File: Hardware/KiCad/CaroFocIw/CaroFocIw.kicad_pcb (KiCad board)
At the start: 4 copper layers, 92 x 42 mm, 111 parts, among them J1 Conn_01x04, J10 Conn_01x03, J11 Conn_01x03, J12 Conn_01x03, J13 Conn_01x03, J14 Conn_01x03, J15 Conn_01x04, J16 Conn_01x04, J17 Conn_01x04, J18 Conn_01x04, J19 Conn_01x04, J2 Conn_01x01, J20 Conn_01x04, J21 Conn_01x02, J22 Conn_01x02, J3 Conn_01x01, J4 Conn_01x01, J5 Conn_01x02, J6 Conn_01x01, J7 Conn_01x02, J8 Conn_01x02, J9 Conn_01x03, Q1 Q_NMOS_SGD, Q2 Q_NMOS_SGD, Q3 Q_NMOS_SGD, Q4 Q_NMOS_SGD, Q5 Q_NMOS_SGD, Q6 Q_NMOS_SGD, U1 TCAN332, U2 STM32F405RGTx, U3 TLE7185-1E, U4 ACS711xEXLT-15AB, U5 AS5048A, U6 ACS711xEXLT-15AB, U7 ACS711xEXLT-15AB, U8 LMR16006YQ3

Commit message: more routing
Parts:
- removed H3, H4: MountingHole_Pad, MountingHole:MountingHole_3.2mm_M3_ISO14580_Pad
- removed J5: Conn_01x02, Pin_Headers:Pin_Header_Straight_1x02_Pitch2.00mm
- removed J6: Conn_01x01, TestPoint:TestPoint_Pad_D3.0mm
- added J23: Conn_01x04, Connector_JST:JST_GH_BM04B-GHS-TBT_1x04-1MP_P1.25mm_Vertical, F.Cu at (217.5, 35.0)
- moved R13 33.4 mm to (168.6, 20.6), turned to 45 degrees
- moved R11 30.8 mm to (147.2, 27.2), turned to 45 degrees
- moved R9 29.9 mm to (166.0, 23.4), turned to 45 degrees
- moved R8 29.5 mm to (148.4, 29.0), turned to 135 degrees
- moved C17 29.0 mm to (170.0, 69.0)
- moved C23 27.0 mm to (150.0, 40.9)
- moved C24 27.0 mm to (147.0, 47.5)
- moved C25 27.0 mm to (152.0, 46.5)
- moved D1 27.0 mm to (150.0, 48.0)
- moved L1 27.0 mm to (151.5, 43.5)
- moved U8 27.0 mm to (147.5, 43.5)
- moved U1 26.4 mm to (163.0, 19.6), turned to 45 degrees
- moved R1 26.1 mm to (164.8, 17.8)
- moved C1 26.1 mm to (161.2, 21.4), turned to 135 degrees
- moved C9 15.9 mm to (172.8, 43.0), turned to 90 degrees
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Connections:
- H1 pad 1: GNDPWR_A -> GND
- H2 pad 1: GNDPWR_A -> GND
- H5 pad 1: Net-(H5-Pad1) -> GND
- H6 pad 1: Net-(H6-Pad1) -> GND
- U1 pad 5: Net-(U1-Pad5) -> (no net)
- U1 pad 8: Net-(U1-Pad8) -> (no net)
- U2 pad 11: Net-(U2-Pad11) -> (no net)
- U2 pad 14: Net-(U2-Pad14) -> (no net)
- U2 pad 15: Net-(U2-Pad15) -> (no net)
- U2 pad 16: Net-(U2-Pad16) -> (no net)
- U2 pad 17: Net-(U2-Pad17) -> (no net)
- U2 pad 2: Net-(U2-Pad2) -> (no net)
- U2 pad 24: Net-(U2-Pad24) -> (no net)
- U2 pad 25: Net-(U2-Pad25) -> (no net)
- U2 pad 26: Net-(U2-Pad26) -> (no net)
- U2 pad 27: Net-(U2-Pad27) -> (no net)
- U2 pad 28: Net-(U2-Pad28) -> (no net)
- U2 pad 29: Net-(U2-Pad29) -> (no net)
- U2 pad 3: Net-(U2-Pad3) -> (no net)
- U2 pad 31: Net-(U2-Pad31) -> (no net)
- U2 pad 33: Net-(U2-Pad33) -> (no net)
- U2 pad 34: /GateDriver/LogicWL -> /GateDriver/LogicUL
- U2 pad 36: /GateDriver/LogicUL -> /GateDriver/LogicWL
- U2 pad 37: Net-(U2-Pad37) -> (no net)
- U2 pad 38: Net-(U2-Pad38) -> (no net)
- U2 pad 39: Net-(U2-Pad39) -> (no net)
- U2 pad 4: Net-(U2-Pad4) -> (no net)
- U2 pad 40: Net-(U2-Pad40) -> (no net)
- U2 pad 41: /MCU/LogicWH -> /MCU/LogicUH
- U2 pad 43: /MCU/LogicUH -> /MCU/LogicWH
- U2 pad 44: Net-(U2-Pad44) -> (no net)
- U2 pad 45: Net-(U2-Pad45) -> (no net)
- U2 pad 47: Net-(U2-Pad47) -> (no net)
- U2 pad 5: Net-(U2-Pad5) -> (no net)
- U2 pad 50: Net-(U2-Pad50) -> (no net)
- U2 pad 51: Net-(U2-Pad51) -> (no net)
- U2 pad 52: Net-(U2-Pad52) -> (no net)
- U2 pad 53: Net-(U2-Pad53) -> (no net)
- U2 pad 54: Net-(U2-Pad54) -> (no net)
- U2 pad 58: Net-(U2-Pad58) -> (no net)
- U2 pad 59: Net-(U2-Pad59) -> (no net)
- U2 pad 6: Net-(U2-Pad6) -> (no net)
- U3 pad 1: GND_B -> (no net)
- U5 pad 10: Net-(U5-Pad10) -> (no net)
- U5 pad 14: Net-(U5-Pad14) -> (no net)
- U5 pad 5: Net-(U5-Pad5) -> (no net)
- U5 pad 6: Net-(U5-Pad6) -> (no net)
- U5 pad 7: Net-(U5-Pad7) -> (no net)
- U5 pad 8: Net-(U5-Pad8) -> (no net)
- U5 pad 9: Net-(U5-Pad9) -> (no net)
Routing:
- net /MCU/CurrentW: track 5.16 -> 43.0 mm, vias 0 -> 1
- net /Can/CanTx: track 33.5 -> 3.76 mm, vias 2 -> 0
- net /MCU/CurrentU: track 4.95 -> 33.0 mm, vias 0 -> 1
- net /Can/CanRx: track 29.5 -> 5.10 mm, vias 2 -> 0
- net /MCU/LogicUH: track 11.2 -> 26.9 mm, vias 0 -> 2
- net /MCU/LogicVH: track 10.9 -> 25.9 mm
- net /MCU/LogicWH: track 10.0 -> 25.1 mm
- net /GateDriver/LogicUL: track 11.7 -> 24.6 mm, vias 0 -> 2
- net /GateDriver/LogicVL: track 11.0 -> 23.7 mm, vias 0 -> 2
- net /GateDriver/LogicWL: track 10.3 -> 22.9 mm, vias 0 -> 2
- net /GateDriver/SourceUL: track 0.00 -> 10.7 mm, vias 0 -> 1
- net /MCU/GateDriverEnable: track 19.6 -> 9.23 mm, vias 0 -> 1
- net Net-(R7-Pad1): track 10.1 -> 1.85 mm, vias 0 -> 1
- net Net-(R6-Pad1): track 9.79 -> 1.89 mm, vias 0 -> 1
- net Net-(R2-Pad2): track 7.44 -> 0.00 mm
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- added copper zone on F.Cu, net GNDA
- removed copper zone on B.Cu, net GNDPWR_A
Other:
- outline, holes or cut-outs redrawn

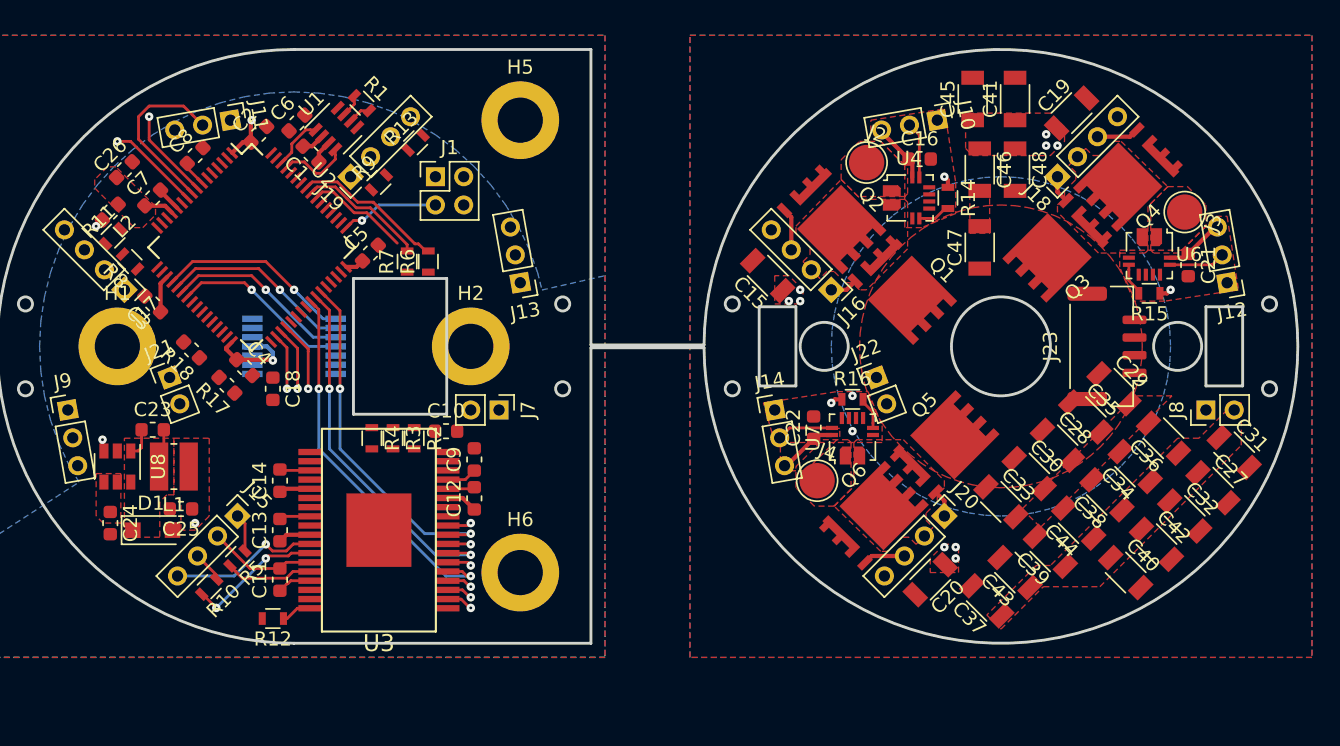
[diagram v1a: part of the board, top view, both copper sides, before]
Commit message: Routing (seems to be) done, should be reviewed before production
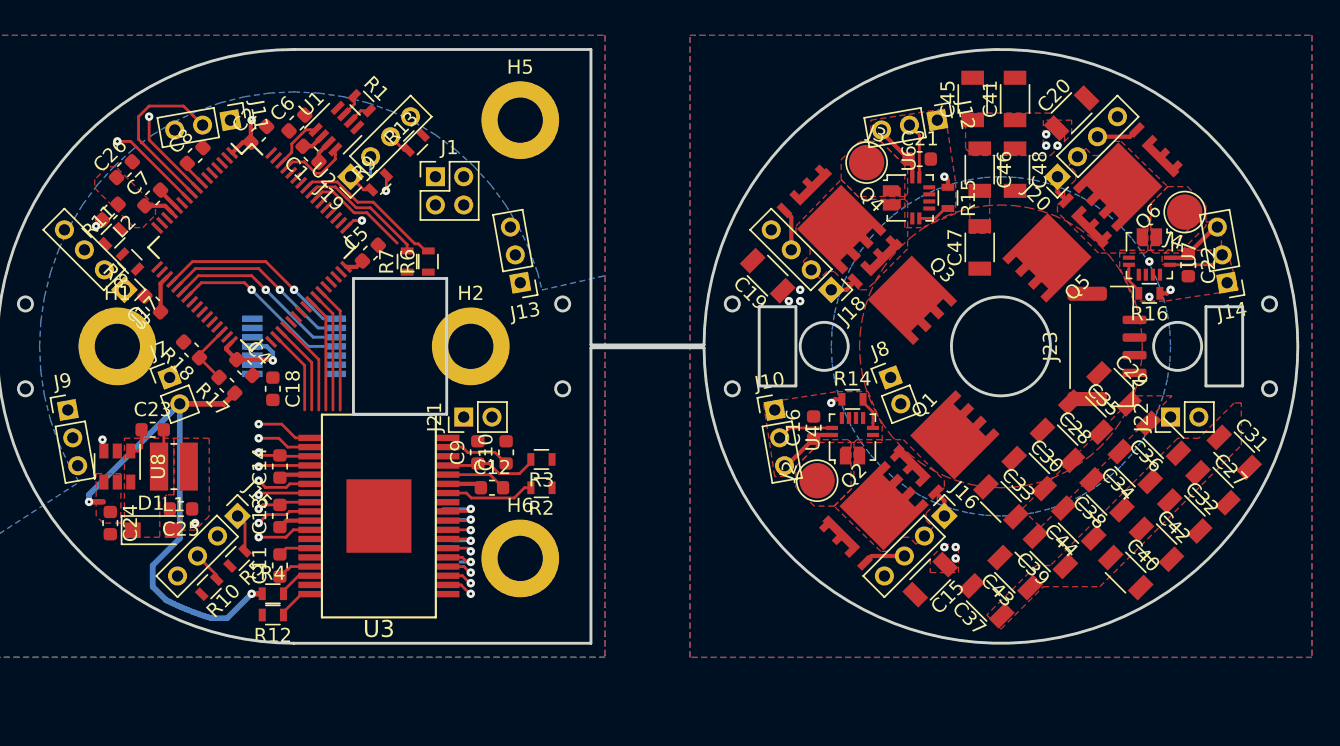
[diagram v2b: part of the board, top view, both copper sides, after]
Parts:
- moved C20 34.5 mm to (215.0, 18.5), turned to 45 degrees
- moved J14 33.2 mm to (226.0, 30.5), turned to 190 degrees
- moved J4 32.2 mm to (223.0, 25.5), turned to 160 degrees
- moved Q6 30.0 mm to (219.0, 23.0), turned to 135 degrees
- moved C22 28.9 mm to (223.2, 29.2), turned to 270 degrees
- moved J20 25.3 mm to (214.0, 23.0), turned to 135 degrees
- moved U7 24.7 mm to (220.5, 28.5), turned to 270 degrees
- moved C15 24.4 mm to (205.0, 51.5), turned to 225 degrees
- moved C19 24.4 mm to (193.5, 30.0), turned to 135 degrees
- moved J10 23.5 mm to (194.0, 39.5), turned to 10 degrees
- moved J12 23.5 mm to (205.5, 19.0), turned to 280 degrees
- moved J7 23.4 mm to (151.2, 37.2), turned to 21 degrees
- moved J2 22.8 mm to (197.0, 44.5), turned to 70 degrees
- moved J3 22.8 mm to (200.5, 22.0), turned to 340 degrees
- moved J8 22.4 mm to (202.2, 37.2), turned to 21 degrees
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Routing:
- net BattA: track 0.00 -> 37.6 mm, vias 0 -> 2
- net /GateDriver/GateWHbR: track 0.00 -> 18.7 mm, vias 0 -> 2
- net /GateDriver/LogicUL: track 24.6 -> 7.74 mm, vias 2 -> 1
- net /MCU/LogicUH: track 26.9 -> 10.6 mm, vias 2 -> 1
- net /MCU/LogicVH: track 25.9 -> 11.4 mm, vias 2 -> 1
- net /GateDriver/LogicVL: track 23.7 -> 9.57 mm, vias 2 -> 1
- net /MCU/LogicWH: track 25.1 -> 12.3 mm, vias 2 -> 1
- net /GateDriver/LogicWL: track 22.9 -> 10.5 mm, vias 2 -> 1
- net /GateDriver/Gate_U_L_bR: track 9.67 -> 0.00 mm, vias 2 -> 0
- net /GateDriver/SourceUL: track 10.7 -> 3.85 mm
- net Net-(R2-Pad2): track 0.00 -> 6.33 mm
- net /GateDriver/GateUHbR: track 6.22 -> 0.00 mm
- net /MCU/SWCLK: track 6.75 -> 1.33 mm
- net /GateDriver/SourceUH: track 7.68 -> 2.32 mm
- net Net-(C9-Pad1): track 2.15 -> 6.77 mm
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
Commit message: forgot to save
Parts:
- removed C29, C35, C36: C, Capacitors_SMD:C_1206
- moved C17 32.6 mm to (160.0, 38.0), turned to 270 degrees
- moved R6 14.5 mm to (178.0, 40.8)
- moved R7 14.5 mm to (176.5, 40.8)
- moved J1 4.00 mm to (170.0, 27.0), turned to 270 degrees
- moved J8 0.95 mm to (201.2, 37.2)
- moved R8 0.43 mm to (148.8, 28.8), turned to 45 degrees
- moved R13 0.18 mm to (168.5, 20.8)
- moved R9 0.15 mm to (166.0, 23.2)
- moved R11 0.07 mm to (147.2, 27.2)
- moved J7 0.07 mm to (151.2, 37.2)
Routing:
- net /MCU/GateDriverEnable: track 9.23 -> 50.5 mm, vias 1 -> 2
- net /Can/CanH: track 1.62 -> 36.8 mm, vias 0 -> 3
- net /Can/CanL: track 1.62 -> 35.9 mm
- net /GateDriver/SourceWL: track 4.04 -> 35.5 mm
- net BattA: track 37.6 -> 68.5 mm, vias 2 -> 4
- net /GateDriver/Gate_W_L_bR: track 3.89 -> 34.7 mm, vias 1 -> 2
- net /GateDriver/SourceWH: track 5.06 -> 32.8 mm
- net /GateDriver/SourceVL: track 3.94 -> 31.0 mm
- net /GateDriver/Gate_V_L_bR: track 3.69 -> 27.5 mm, vias 1 -> 2
- net /GateDriver/SourceVH: track 3.83 -> 27.6 mm
- net /GateDriver/GateVHbR: track 3.98 -> 27.5 mm, vias 1 -> 2
- net /MCU/~RST: track 1.82 -> 22.2 mm, vias 0 -> 1
- net Net-(R7-Pad1): track 1.85 -> 22.1 mm, vias 1 -> 0
- net Net-(R6-Pad1): track 1.89 -> 21.9 mm, vias 1 -> 0
- net /MCU/~GateDriverErr1: track 9.11 -> 27.5 mm
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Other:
- outline, holes or cut-outs redrawn

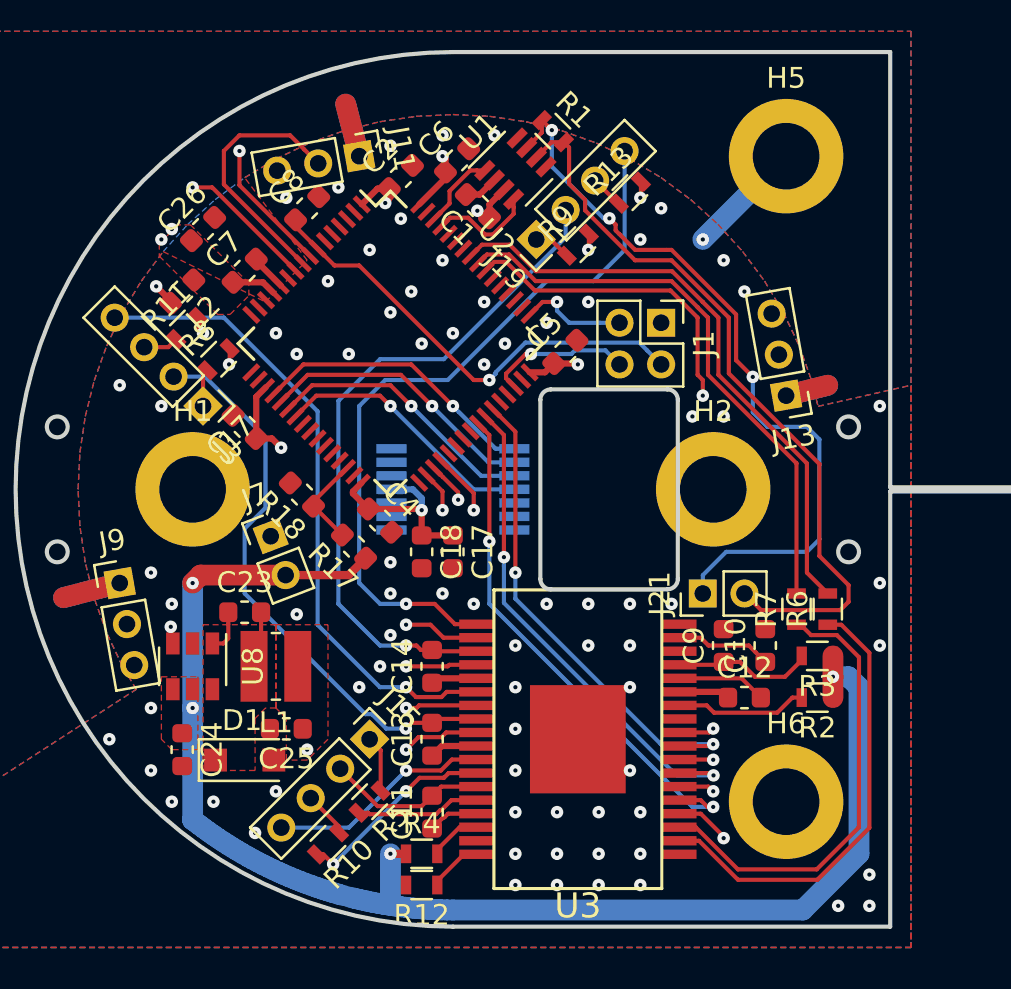
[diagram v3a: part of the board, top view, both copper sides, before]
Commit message: routing done, some via stitching and panelizing to do
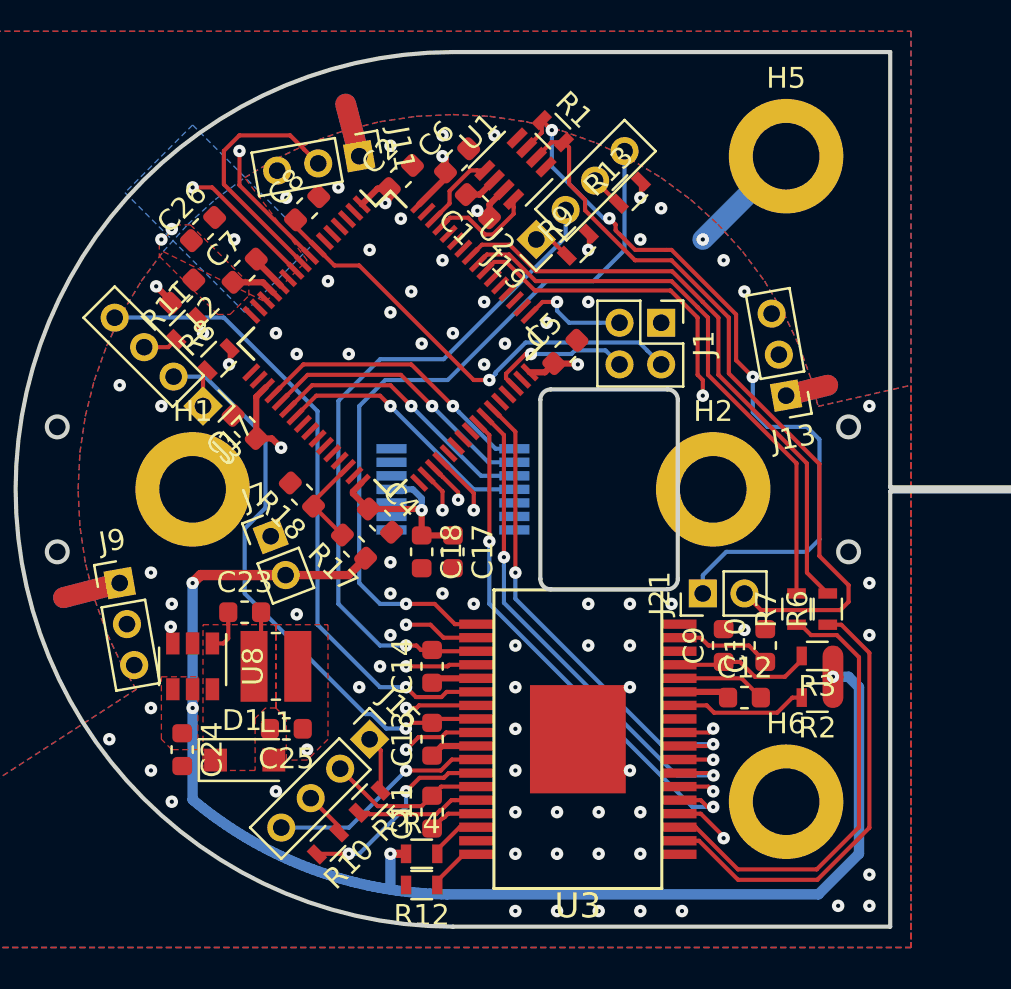
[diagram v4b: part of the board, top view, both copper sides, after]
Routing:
- net BattA: track 68.5 -> 66.8 mm
- net /MCU/CurrentU: track 33.0 -> 31.9 mm
- net +3.3VA: track 5.06 -> 4.50 mm
- net GNDA: vias 0 -> 1
- net GND: vias 77 -> 74

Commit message: some panelizing
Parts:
- moved C15 6.00 mm to (199.0, 51.5)
- moved C16 6.00 mm to (190.8, 40.8)
- moved C19 6.00 mm to (187.5, 30.0)
- moved C20 6.00 mm to (209.0, 18.5)
- moved C21 6.00 mm to (198.2, 21.8)
- moved C22 6.00 mm to (217.2, 29.2)
- moved C27 6.00 mm to (219.0, 45.0)
- moved C28 6.00 mm to (208.0, 42.0)
- moved C30 6.00 mm to (206.0, 44.0)
- moved C31 6.00 mm to (220.5, 42.5)
- moved C32 6.00 mm to (217.0, 47.0)
- moved C33 6.00 mm to (204.0, 46.0)
- moved C34 6.00 mm to (213.5, 43.5)
- moved C37 6.00 mm to (203.0, 53.0)
- moved C38 6.00 mm to (211.5, 45.5)
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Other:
- board size 92 x 42 mm -> 86 x 42 mm

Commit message: preliminary version 1.0
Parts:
- removed the C31 at (220.5, 42.5)
- removed the C37 at (203.0, 53.0)
- removed the C41 at (205.0, 17.5)
- removed H5, H6: MountingHole_Pad, MountingHole:MountingHole_3.2mm_M3_ISO14580_Pad
- removed J21: Conn_01x02, Connector_PinHeader_2.00mm:PinHeader_1x02_P2.00mm_Vertical
- removed J23: Conn_01x04, Connector_JST:JST_GH_BM04B-GHS-TBT_1x04-1MP_P1.25mm_Vertical
- removed the J8 at (195.2, 37.2)
- removed the U1 at (163.0, 19.6)
- removed the U8 at (147.5, 43.5)
- added C29: 10µ 35V, Capacitor_SMD:C_1206_3216Metric, F.Cu at (46.0, 9.00)
- added C34: 10µ 35V, Capacitor_SMD:C_1206_3216Metric, F.Cu at (43.0, 18.0)
- added C38: 10µ 35V, Capacitor_SMD:C_1206_3216Metric, F.Cu at (45.0, -17.5)
- added G***: LOGO, libs:CDLC-Logo, B.Cu at (53.0, 16.0)
- added H3: MountingHole_Pad, MountingHole:MountingHole_3.2mm_M3_ISO14580_Pad, F.Cu at (16.0, -16.0)
- added H4: MountingHole_Pad, MountingHole:MountingHole_3.2mm_M3_ISO14580_Pad, F.Cu at (16.0, 16.0)
- added J2: Conn_01x01, TestPoint:TestPoint_Pad_D2.5mm, F.Cu at (34.5, -13.0)
- added J5: Conn_01x02, Connector_PinHeader_2.00mm:PinHeader_1x02_P2.00mm_Vertical, F.Cu at (-8.75, 2.25)
- added J6: Conn_01x02, Connector_PinHeader_2.00mm:PinHeader_1x02_P2.00mm_Vertical, F.Cu at (35.2, 2.25)
- added NT1: Net-Tie_2, NetTie:NetTie-2_SMD_Pad0.5mm, B.Cu at (-8.25, -10.2)
- added REF**: OSHW-Logo2_7.3x6mm_SilkScreen, Symbol:OSHW-Logo2_7.3x6mm_SilkScreen, B.Cu at (51.0, 4.00)
- added U5: ACS711xEXLT-15AB, Sensor_Current:Allegro_QFN-12-10-1EP_3x3mm_P0.5mm, F.Cu at (33.5, 6.50)
- added U9: LMR16006YQ3, Package_TO_SOT_SMD:SOT-23-6, F.Cu at (-12.5, 8.50)
- C10: value 2,2µ -> 4.7µ 25V
- C11, C12, C13, C14: value 1µ -> 4.7µ 25V
- C15, C19, C20: value 22μ, 25V -> 10μ 35V; footprint Capacitors_SMD:C_1206 -> Capacitor_SMD:C_1206_3216Metric
- C18, C25, C26: value 10μ -> 10μ 6.3V
- C2, C3, C4, C5, C6: value 2.2μ -> 4.7µ, 6.3V
- C24: value 10μ -> 10μ 35V
- C27, C28, C30: value C -> 10µ 35V; footprint Capacitors_SMD:C_1206 -> Capacitor_SMD:C_1206_3216Metric
- C31: renamed from C32; value C -> 10µ 35V; footprint Capacitors_SMD:C_1206 -> Capacitor_SMD:C_1206_3216Metric
- C32: renamed from C33; value C -> 10µ 35V; footprint Capacitors_SMD:C_1206 -> Capacitor_SMD:C_1206_3216Metric
- C33: renamed from C34; value C -> 10µ 35V; footprint Capacitors_SMD:C_1206 -> Capacitor_SMD:C_1206_3216Metric
- C35: renamed from C38; value C -> 10µ 35V; footprint Capacitors_SMD:C_1206 -> Capacitor_SMD:C_1206_3216Metric
- C36: renamed from C39; value C -> 10µ 35V; footprint Capacitors_SMD:C_1206 -> Capacitor_SMD:C_1206_3216Metric
- C37: renamed from C40; value C -> 10µ 35V; footprint Capacitors_SMD:C_1206 -> Capacitor_SMD:C_1206_3216Metric
- C39: renamed from C42; value C -> 10µ 35V; footprint Capacitors_SMD:C_1206 -> Capacitor_SMD:C_1206_3216Metric
- C40: renamed from C43; value C -> 10µ 35V; footprint Capacitors_SMD:C_1206 -> Capacitor_SMD:C_1206_3216Metric
- C41: renamed from C44; value C -> 10µ 35V; footprint Capacitors_SMD:C_1206 -> Capacitor_SMD:C_1206_3216Metric
- C42: renamed from C45; value C -> 10µ 35V; footprint Capacitors_SMD:C_1206 -> Capacitor_SMD:C_1206_3216Metric
- C43: renamed from C46; value C -> 10µ 35V; footprint Capacitors_SMD:C_1206 -> Capacitor_SMD:C_1206_3216Metric
- C44: renamed from C47; value C -> 10µ 35V; footprint Capacitors_SMD:C_1206 -> Capacitor_SMD:C_1206_3216Metric
- C45: renamed from C48; value C -> 10µ 35V; footprint Capacitors_SMD:C_1206 -> Capacitor_SMD:C_1206_3216Metric
- C7: value 10μ -> 4.7µ, 6.3V
- C9: value 2,2µ -> 4.7µ 35V
- D1: footprint Diodes_SMD:D_SOD-123F -> Diode_SMD:D_SOD-123F
- J13: value Conn_01x03 -> Conn_01x04; footprint Connector_PinHeader_2.00mm:PinHeader_1x03_P2.00mm_Vertical -> Connector_PinHeader_2.00mm:PinHeader_1x04_P2.00mm_Vertical
- J19: value Conn_01x04 -> Conn_01x02; footprint Connector_PinHeader_2.00mm:PinHeader_1x04_P2.00mm_Vertical -> Connector_PinHeader_2.00mm:PinHeader_1x02_P2.00mm_Vertical
- J4: value Conn_01x01 -> Conn_01x04_MountingPin; footprint TestPoint:TestPoint_Pad_D2.5mm -> Connector_JST:JST_GH_BM04B-GHS-TBT_1x04-1MP_P1.25mm_Vertical
- J7: value Conn_01x02 -> Conn_01x03; footprint Connector_PinHeader_2.00mm:PinHeader_1x02_P2.00mm_Vertical -> Connector_PinHeader_2.00mm:PinHeader_1x03_P2.00mm_Vertical
- L1: footprint Inductors_SMD:L_Wuerth_MAPI-3015 -> Inductor_SMD:L_Wuerth_MAPI-3015
- Q1, Q2, Q3, Q4, Q5, Q6: value Q_NMOS_SGD -> BSZ013NE2LS5I; footprint libs:TDSON-8_FL -> libs:PG-TSDSON-8-FL
- R1, R10, R11, R12, R13, R14, R15, R16, R2, R3, R4, R5, R8, R9: footprint Resistors_SMD:R_0603 -> Resistor_SMD:R_0603_1608Metric
- R6, R7: value 4.7k -> 10k; footprint Resistors_SMD:R_0603 -> Resistor_SMD:R_0603_1608Metric
- U2: value STM32F405RGTx -> TCAN332; footprint Package_QFP:LQFP-64_10x10mm_P0.5mm -> Package_TO_SOT_SMD:SOT-23-8
- U3: value TLE7185-1E -> STM32F405RGTx; footprint libs:PG-DSO-36-38 -> Package_QFP:LQFP-64_10x10mm_P0.5mm
- U4: value ACS711xEXLT-15AB -> TLE7185-1E; footprint Sensor_Current:Allegro_QFN-12-10-1EP_3x3mm_P0.5mm -> libs:PG-DSO-36-38
- moved U4 189.8 mm to (6.00, 12.0)
- moved J13 180.9 mm to (-4.00, 12.0), turned to 315 degrees
- moved U3 177.4 mm to (-3.00, -7.00), turned to 315 degrees
- moved J15 175.6 mm to (-12.0, -4.00), turned to 225 degrees
- moved J7 170.4 mm to (-16.0, 4.50), turned to 10 degrees
- moved J4 167.5 mm to (51.5, 0.00), turned to 90 degrees
- moved Q3 165.0 mm to (36.0, -5.00), turned to 135 degrees
- moved Q1 164.6 mm to (39.0, 8.00), turned to 225 degrees
- moved Q4 164.0 mm to (31.8, -9.21), turned to 135 degrees
- moved Q2 163.9 mm to (34.8, 12.2), turned to 225 degrees
- moved C19 163.8 mm to (27.5, -5.30)
- moved C1 163.8 mm to (1.20, -13.6)
- moved C10 163.8 mm to (15.0, 7.50)
- moved C11 163.8 mm to (-1.00, 15.5)
- moved C12 163.8 mm to (14.0, 10.0)
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- renumbered J12 to J10, J14 to J12, J16 to J14, J18 to J16, J20 to J18, J22 to J20, J10 to J8, J2 to U1, U5 to U6, U6 to U7, U7 to U8
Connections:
- J11 pad 2: /MCU/CurrentV -> /MCU/CurrentW
- J13 pad 1: GNDA -> /GateDriver/GateUH
- J13 pad 2: /MCU/CurrentW -> /GateDriver/SourceUH
- J13 pad 3: +3.3VA -> /GateDriver/GateUL
- J15 pad 1: /GateDriver/GateUH -> /GateDriver/GateVH
- J15 pad 2: /GateDriver/SourceUH -> /GateDriver/SourceVH
- J15 pad 3: /GateDriver/GateUL -> /GateDriver/GateVL
- J15 pad 4: /GateDriver/SourceUL -> /GateDriver/SourceVL
- J17 pad 1: /GateDriver/GateVH -> /GateDriver/GateWH
- J17 pad 2: /GateDriver/SourceVH -> /GateDriver/SourceWH
- J17 pad 3: /GateDriver/GateVL -> /GateDriver/GateWL
- J17 pad 4: /GateDriver/SourceVL -> /GateDriver/SourceWL
- J19 pad 1: /GateDriver/GateWH -> /Can/CanH
- J19 pad 2: /GateDriver/SourceWH -> /Can/CanL
- J3 pad 1: /CurrentSensingV/PhaseOut -> /CurrentsensingW/PhaseOut
- J4 pad 1: /CurrentsensingW/PhaseOut -> GNDPWR
- J7 pad 1: GND -> GNDA
- J7 pad 2: BattA -> /MCU/CurrentU
- J9 pad 2: /MCU/CurrentU -> /MCU/CurrentV
- U2 pad 1: +3V3 -> /Can/CanTx
- U2 pad 2: (no net) -> GND
- U2 pad 3: (no net) -> +3V3
- U2 pad 4: (no net) -> /Can/CanRx
- U2 pad 6: (no net) -> /Can/CanL
- U2 pad 7: /MCU/~RST -> /Can/CanH
- U2 pad 8: /MCU/CurrentW -> (no net)
- U3 pad 1: (no net) -> +3V3
- U3 pad 10: /GateDriver/LogicWL -> /MCU/CurrentU
- U3 pad 11: GND -> (no net)
- U3 pad 12: Net-(R2-Pad2) -> GNDA
- U3 pad 13: Net-(C12-Pad1) -> +3.3VA
- U3 pad 14: Net-(C12-Pad2) -> (no net)
- U3 pad 15: Net-(C9-Pad1) -> (no net)
- U3 pad 16: GND -> (no net)
- U3 pad 17: Net-(C10-Pad1) -> (no net)
- U3 pad 19: /GateDriver/SourceWL -> +3V3
- U3 pad 2: Net-(R6-Pad1) -> (no net)
- U3 pad 20: /GateDriver/Gate_W_L_bR -> /Encoder/~EncoderCs
- U3 pad 21: /GateDriver/SourceWH -> /Encoder/EncoderSclk
- U3 pad 22: /GateDriver/GateWHbR -> /Encoder/EncoderMiso
- U3 pad 23: Net-(C14-Pad1) -> /Encoder/EncoderMosi
- U3 pad 24: /GateDriver/SourceVL -> (no net)
- U3 pad 25: /GateDriver/Gate_V_L_bR -> (no net)
- U3 pad 26: /GateDriver/SourceVH -> (no net)
- U3 pad 27: /GateDriver/GateVHbR -> (no net)
- U3 pad 28: Net-(C13-Pad1) -> (no net)
- U3 pad 29: /GateDriver/SourceUL -> (no net)
- U3 pad 3: Net-(R7-Pad1) -> (no net)
- U3 pad 30: /GateDriver/Gate_U_L_bR -> /DcLinkVoltageSensing/AnalogOut
- U3 pad 31: /GateDriver/SourceUH -> (no net)
- U3 pad 32: /GateDriver/GateUHbR -> +3V3
- U3 pad 33: Net-(C11-Pad1) -> (no net)
- U3 pad 34: Net-(R4-Pad2) -> /GateDriver/LogicUL
- U3 pad 35: GND -> /GateDriver/LogicVL
- U3 pad 36: Net-(R12-Pad1) -> /GateDriver/LogicWL
- U3 pad 37: GND -> (no net)
- U3 pad 4: /MCU/GateDriverEnable -> (no net)
- U3 pad 5: /MCU/LogicUH -> (no net)
- U3 pad 6: /GateDriver/LogicUL -> (no net)
- U3 pad 7: /MCU/LogicVH -> /MCU/~RST
- U3 pad 8: /GateDriver/LogicVL -> /MCU/CurrentW
- U3 pad 9: /MCU/LogicWH -> /MCU/CurrentV
- U4 pad 1: /CurrentSensingU/PhaseOut -> (no net)
- U4 pad 10: 3.3VA_U -> /GateDriver/LogicWL
- U4 pad 2: /CurrentSensingU/PhaseIn -> Net-(R6-Pad1)
- U4 pad 3: AGND_U -> Net-(R7-Pad1)
- U4 pad 4: Net-(R14-Pad2) -> /MCU/GateDriverEnable
- U4 pad 5: AGND_U -> /MCU/LogicUH
- U4 pad 6: AGND_U -> /GateDriver/LogicUL
- U4 pad 7: AGND_U -> /MCU/LogicVH
- U4 pad 8: AGND_U -> /GateDriver/LogicVL
- U4 pad 9: /CurrentSensingU/AnalogOut -> /MCU/LogicWH
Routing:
- net GNDA: track 24.1 -> 16.8 mm, vias 1 -> 38
- net /GateDriver/LogicWL: track 22.9 -> 25.4 mm
- net /MCU/GateDriverEnable: track 50.5 -> 52.7 mm
- net /Can/CanH: track 36.8 -> 38.5 mm
- net /GateDriver/SourceWL: track 35.5 -> 36.7 mm
- net /Can/CanL: track 35.9 -> 37.0 mm
- net GNDPWR: track 0.55 -> 1.50 mm, vias 0 -> 51
- net /MCU/SWDIO: track 7.01 -> 7.91 mm
- net /HalfBridgeU/GateH: track 1.95 -> 2.84 mm
- net /HalfBridgeV/GateH: track 1.95 -> 2.84 mm
- net /HalfBridgeW/GateH: track 1.95 -> 2.84 mm
- net +3V3: track 25.4 -> 26.2 mm
- net Net-(R6-Pad1): track 21.9 -> 22.6 mm
- net /GateDriver/Gate_W_L_bR: track 34.7 -> 35.4 mm
- net GND: track 7.29 -> 7.50 mm, vias 74 -> 83
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- added copper zone on B.Cu, net (none)
- added copper zone on F.Cu, net (none)
- added copper zone on In1.Cu, net (none)
- added copper zone on In2.Cu, net (none)
- added copper zone on In2.Cu, net +3.3VA
- added copper zone on In1.Cu, net GNDA
- removed copper zone on In1.Cu, net +3.3VA
- removed copper zone on In2.Cu, net GNDA
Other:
- board size 86 x 42 mm -> 85 x 42 mm
- board text added: "09/2019"
- board text added: "3V3A"
- board text added: "AGND"
- board text added: "Batt"
- board text added: "CanH"
- board text added: "CanL"
- board text added: "CaroFocIW Version 1.0"
- board text added: "CrrntSns"
- board text added: "GND"
- board text added: "GateH"
- board text added: "GateL"
- board text added: "JLCJLCJLCJLC"
- board text added: "SWCLK"
- board text added: "SWDIO"
- board text added: "SourceH"
- board text added: "SourceL"
- board text added: "Supply+"
- board text added: "Supply-"
- board text added: "U"
- board text added: "V"
- board text added: "W"
- board text added: "designed by O. H. Maier 09/2019"
- board text added: "~RST"
